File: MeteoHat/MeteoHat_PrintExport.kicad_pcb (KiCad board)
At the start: 2 copper layers, 205 x 129 mm, 36 parts, among them J1 RaspberryPI, SW1 SW_Push, U1 BME680, U2 BH1750

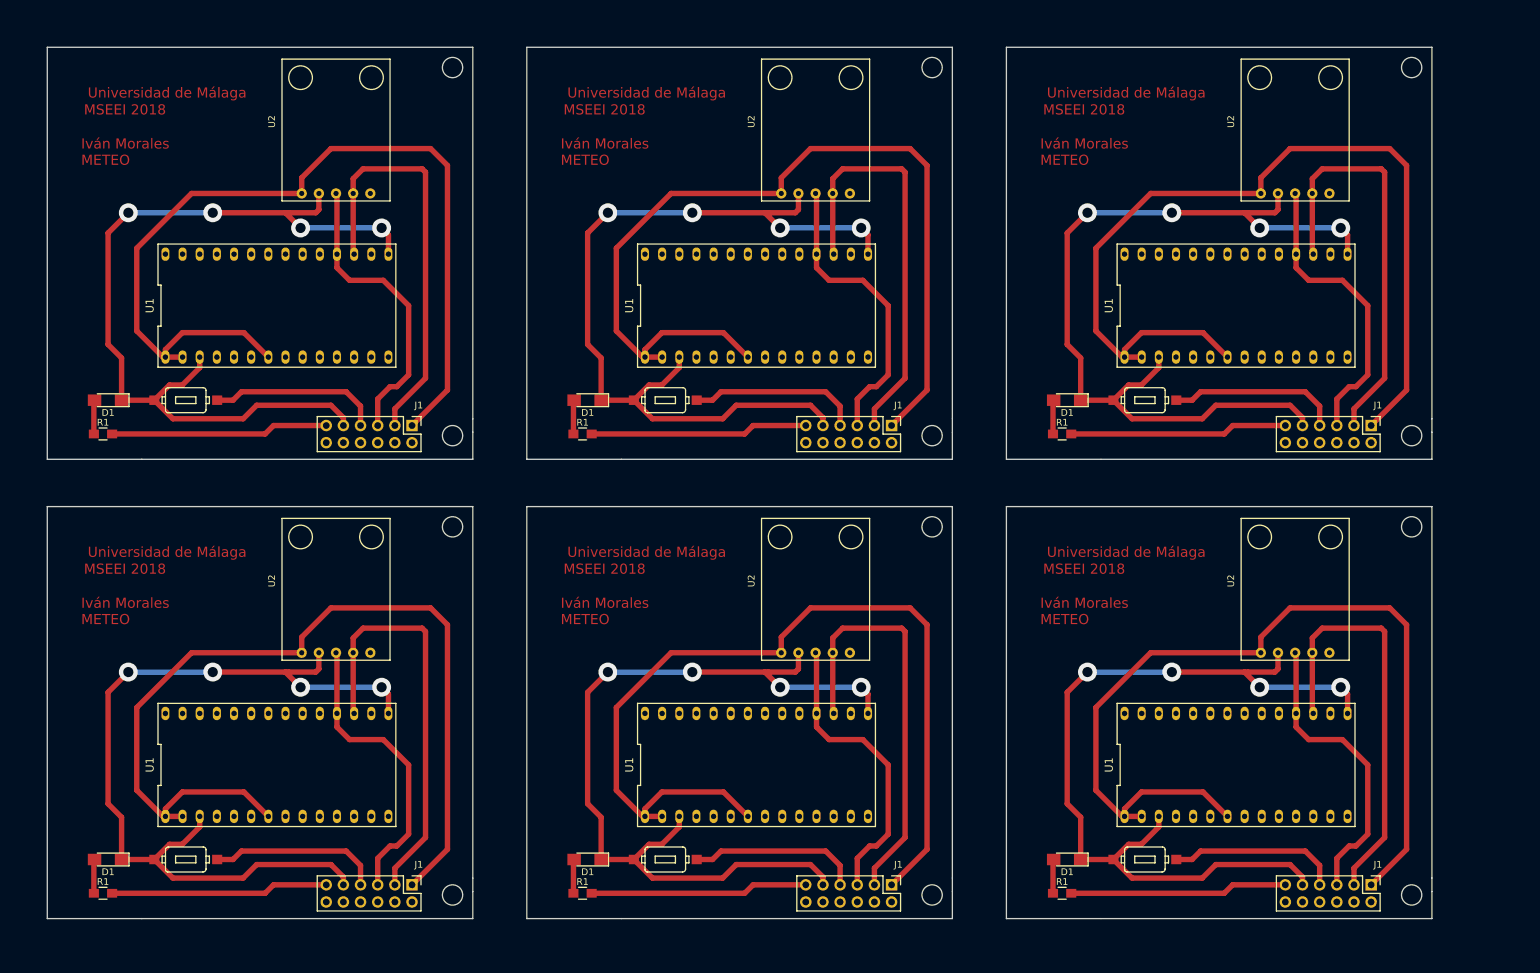
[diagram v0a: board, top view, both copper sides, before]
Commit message: Added PCB Keepout Zones
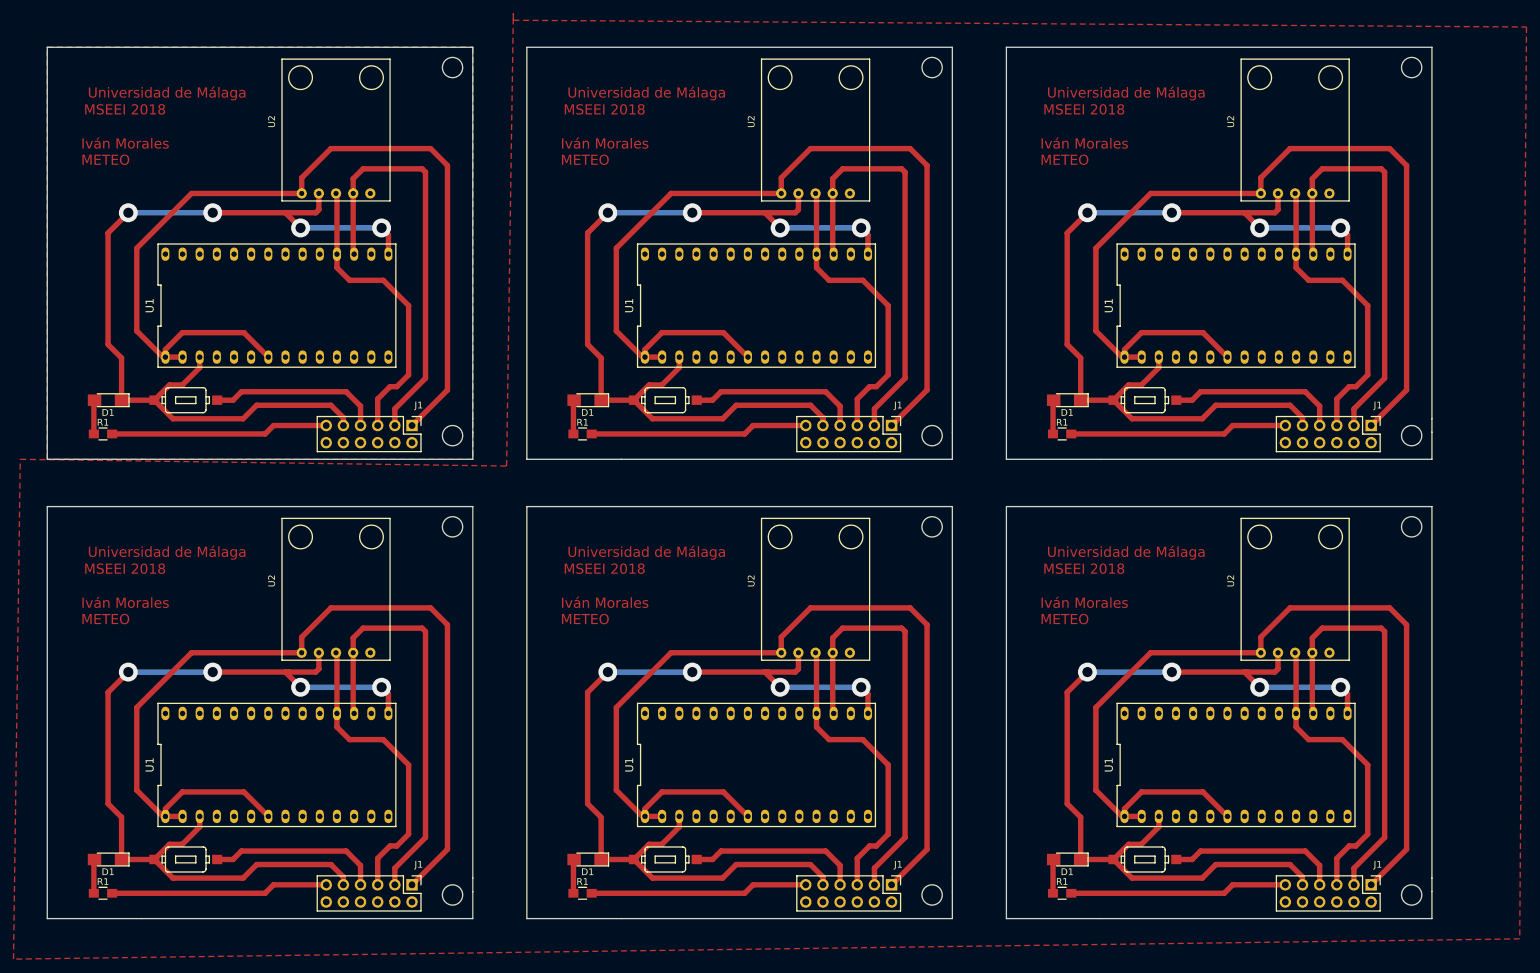
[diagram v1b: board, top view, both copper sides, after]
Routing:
- added copper zone on F.Cu, net GND
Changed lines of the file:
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@@
     (nets 36)
   )
-  (page USLetter)
+  (page A4)
   (title_block
     (title "METEO Hat for Raspberry PI 3")
@@
     (last_trace_width 0.8)
     (trace_clearance 0.2)
-    (zone_clearance 0.508)
+    (zone_clearance 1.2)
     (zone_45_only no)
     (trace_min 0.2)
@@
     (pad_to_mask_clearance 0.2)
     (aux_axis_origin 0 0)
-    (visible_elements FFFFEF7F)
+    (visible_elements 7FFFFFFF)
     (pcbplotparams
       (layerselection 0x01000_00000001)
@@
   (segment (start 61.5 80) (end 69.3 80) (width 0.8) (layer F.Cu) (net 34))
   (segment (start 60.25 81.25) (end 61.5 80) (width 0.8) (layer F.Cu) (net 34))
+  (zone (net 4) (net_name GND) (layer F.Cu) (hatch edge 0.508)
+    (connect_pads (clearance 1.2))
+    (min_thickness 0.508)
+    (fill yes (arc_segments 16) (thermal_gap 1.2) (thermal_bridge_width 1.2) (smoothing chamfer) (radius 0.5))
+    (polygon
+      (pts
+        (xy 91 85) (xy 28 85) (xy 28 24) (xy 91 24)
+      )
+    )
+  )
+  (zone (net 4) (net_name GND) (layer F.Cu) (hatch edge 0.508)
+    (connect_pads (clearance 1.2))
+    (min_thickness 0.508)
+    (fill yes (arc_segments 16) (thermal_gap 1.2) (thermal_bridge_width 1.2) (smoothing chamfer) (radius 0.5))
+    (polygon
+      (pts
+        (xy 97 20) (xy 247 21) (xy 246 156) (xy 23 159) (xy 24 85)
+        (xy 96 86) (xy 97 19)
+      )
+    )
+  )
 )
